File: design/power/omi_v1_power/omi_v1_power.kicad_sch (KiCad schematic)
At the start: 0 parts

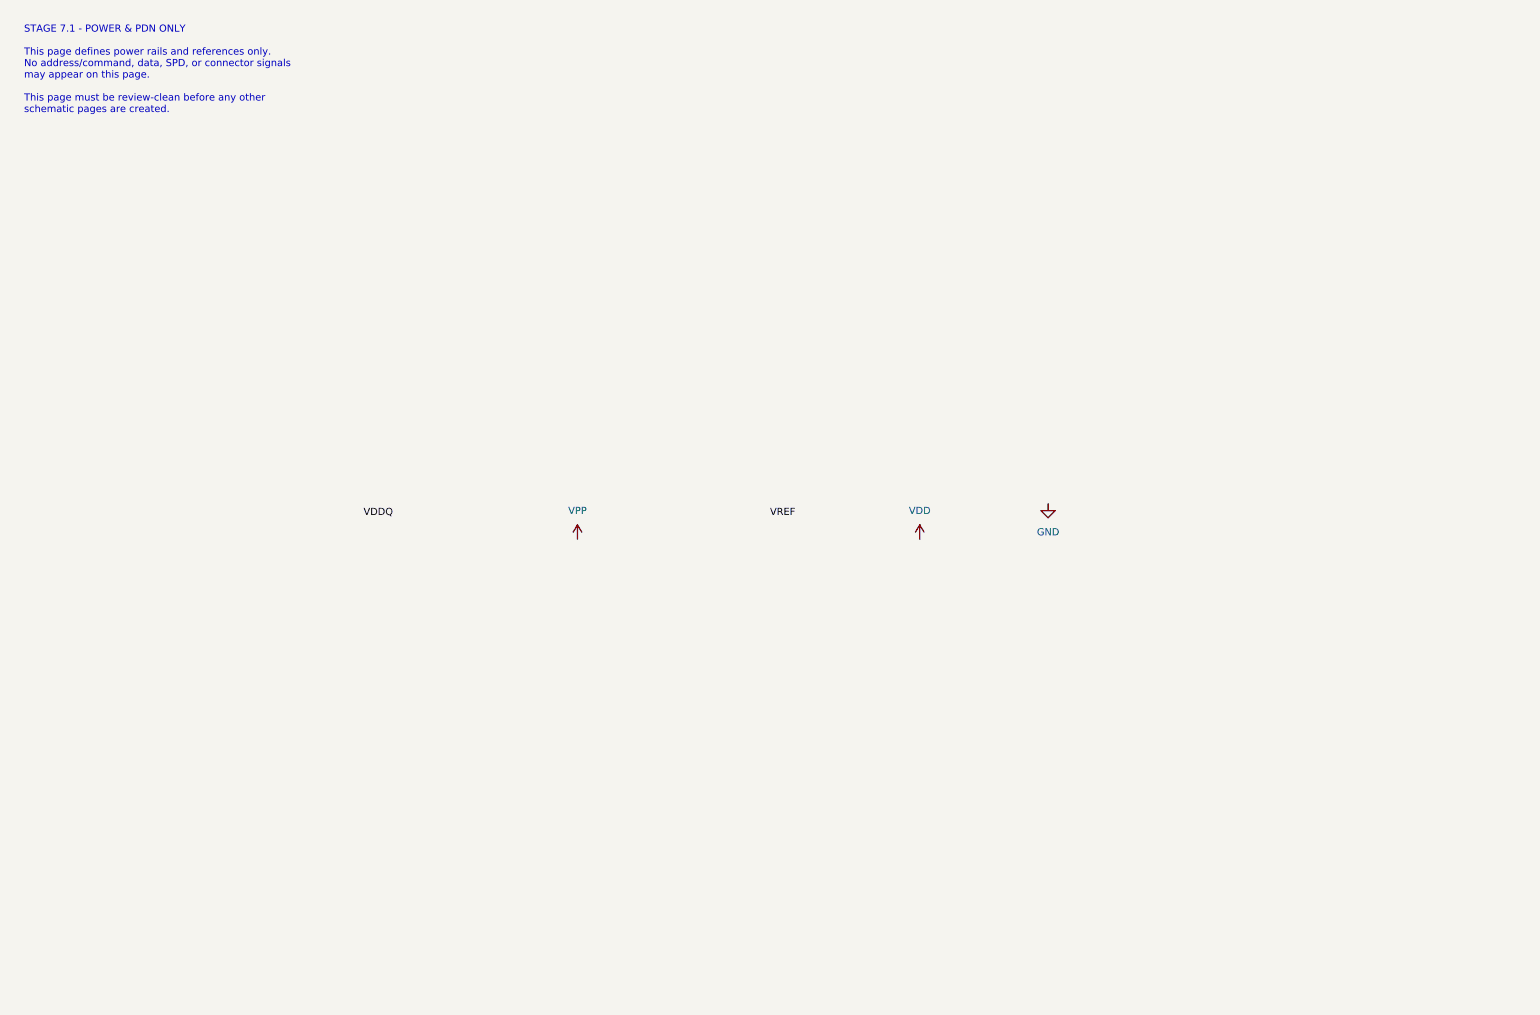
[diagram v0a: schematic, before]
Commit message: feat: add initial OMI v1 power and PDN schematic with PDF documentation
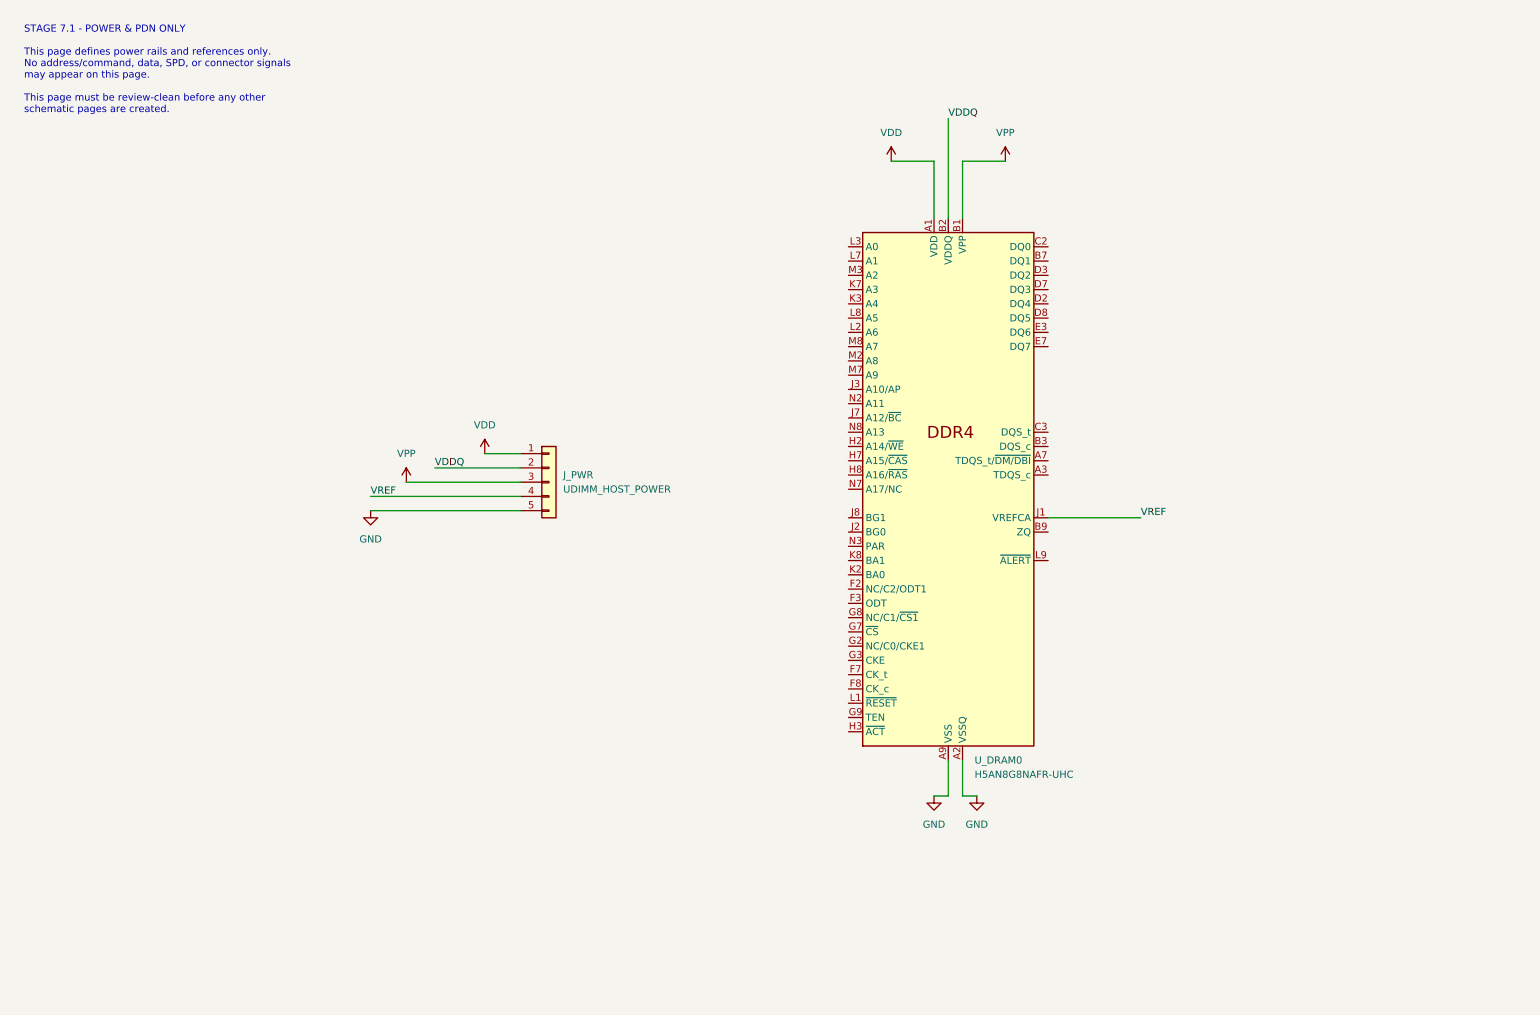
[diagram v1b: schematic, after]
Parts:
- added J_PWR: UDIMM_HOST_POWER, symbol Connector_Generic:Conn_01x05
- added U_DRAM0: H5AN8G8NAFR-UHC, Package_BGA:FBGA-78_7.5x11mm_Layout2x3x13_P0.8mm, symbol Memory_RAM:H5AN8G8NAFR-UHC
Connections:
- net GND: now also J_PWR.5 (Pin_5), U_DRAM0.A2 (VSSQ), U_DRAM0.A8 (VSSQ), U_DRAM0.A9 (VSS), U_DRAM0.C8 (VSS), U_DRAM0.D1 (VSSQ), U_DRAM0.D9 (VSSQ), U_DRAM0.E1 (VSS), U_DRAM0.E9 (VSS), U_DRAM0.G1 (VSS), U_DRAM0.H9 (VSS), U_DRAM0.K1 (VSS), U_DRAM0.K9 (VSS), U_DRAM0.N1 (VSS)
- net VDD: now also J_PWR.1 (Pin_1), U_DRAM0.A1 (VDD), U_DRAM0.C7 (VDD), U_DRAM0.F1 (VDD), U_DRAM0.F9 (VDD), U_DRAM0.H1 (VDD), U_DRAM0.J9 (VDD), U_DRAM0.M1 (VDD), U_DRAM0.N9 (VDD)
- net VDDQ: now also J_PWR.2 (Pin_2), U_DRAM0.B2 (VDDQ), U_DRAM0.B8 (VDDQ), U_DRAM0.C1 (VDDQ), U_DRAM0.C9 (VDDQ), U_DRAM0.E2 (VDDQ), U_DRAM0.E8 (VDDQ)
- net VPP: now also J_PWR.3 (Pin_3), U_DRAM0.B1 (VPP), U_DRAM0.M9 (VPP)
- net VREF: now also J_PWR.4 (Pin_4), U_DRAM0.J1 (VREFCA)

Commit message: feat: Add OMI v1 Stage 7.1 Power & PDN final documentation and PDF artifact.
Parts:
- added U_DRAM1, U_DRAM2, U_DRAM3, U_DRAM4, U_DRAM5, U_DRAM6, U_DRAM7: H5AN8G8NAFR-UHC, Package_BGA:FBGA-78_7.5x11mm_Layout2x3x13_P0.8mm, symbol Memory_RAM:H5AN8G8NAFR-UHC
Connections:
- net GND: now also U_DRAM1.A2 (VSSQ), U_DRAM1.A8 (VSSQ), U_DRAM1.A9 (VSS), U_DRAM1.C8 (VSS), U_DRAM1.D1 (VSSQ), U_DRAM1.D9 (VSSQ), U_DRAM1.E1 (VSS), U_DRAM1.E9 (VSS), U_DRAM1.G1 (VSS), U_DRAM1.H9 (VSS), U_DRAM1.K1 (VSS), U_DRAM1.K9 (VSS), U_DRAM1.N1 (VSS), U_DRAM2.A2 (VSSQ), U_DRAM2.A8 (VSSQ), U_DRAM2.A9 (VSS), U_DRAM2.C8 (VSS), U_DRAM2.D1 (VSSQ), U_DRAM2.D9 (VSSQ), U_DRAM2.E1 (VSS), U_DRAM2.E9 (VSS), U_DRAM2.G1 (VSS), U_DRAM2.H9 (VSS), U_DRAM2.K1 (VSS), U_DRAM2.K9 (VSS), U_DRAM2.N1 (VSS), U_DRAM3.A2 (VSSQ), U_DRAM3.A8 (VSSQ), U_DRAM3.A9 (VSS), U_DRAM3.C8 (VSS), U_DRAM3.D1 (VSSQ), U_DRAM3.D9 (VSSQ), U_DRAM3.E1 (VSS), U_DRAM3.E9 (VSS), U_DRAM3.G1 (VSS), U_DRAM3.H9 (VSS), U_DRAM3.K1 (VSS), U_DRAM3.K9 (VSS), U_DRAM3.N1 (VSS), U_DRAM4.A2 (VSSQ), U_DRAM4.A8 (VSSQ), U_DRAM4.A9 (VSS), U_DRAM4.C8 (VSS), U_DRAM4.D1 (VSSQ), U_DRAM4.D9 (VSSQ), U_DRAM4.E1 (VSS), U_DRAM4.E9 (VSS), U_DRAM4.G1 (VSS), U_DRAM4.H9 (VSS), U_DRAM4.K1 (VSS), U_DRAM4.K9 (VSS), U_DRAM4.N1 (VSS), U_DRAM5.A2 (VSSQ), U_DRAM5.A8 (VSSQ), U_DRAM5.A9 (VSS), U_DRAM5.C8 (VSS), U_DRAM5.D1 (VSSQ), U_DRAM5.D9 (VSSQ), U_DRAM5.E1 (VSS), U_DRAM5.E9 (VSS), U_DRAM5.G1 (VSS), U_DRAM5.H9 (VSS), U_DRAM5.K1 (VSS), U_DRAM5.K9 (VSS), U_DRAM5.N1 (VSS), U_DRAM6.A2 (VSSQ), U_DRAM6.A8 (VSSQ), U_DRAM6.A9 (VSS), U_DRAM6.C8 (VSS), U_DRAM6.D1 (VSSQ), U_DRAM6.D9 (VSSQ), U_DRAM6.E1 (VSS), U_DRAM6.E9 (VSS), U_DRAM6.G1 (VSS), U_DRAM6.H9 (VSS), U_DRAM6.K1 (VSS), U_DRAM6.K9 (VSS), U_DRAM6.N1 (VSS), U_DRAM7.A2 (VSSQ), U_DRAM7.A8 (VSSQ), U_DRAM7.A9 (VSS), U_DRAM7.C8 (VSS), U_DRAM7.D1 (VSSQ), U_DRAM7.D9 (VSSQ), U_DRAM7.E1 (VSS), U_DRAM7.E9 (VSS), U_DRAM7.G1 (VSS), U_DRAM7.H9 (VSS), U_DRAM7.K1 (VSS), U_DRAM7.K9 (VSS), U_DRAM7.N1 (VSS)
- net VDD: now also U_DRAM1.A1 (VDD), U_DRAM1.C7 (VDD), U_DRAM1.F1 (VDD), U_DRAM1.F9 (VDD), U_DRAM1.H1 (VDD), U_DRAM1.J9 (VDD), U_DRAM1.M1 (VDD), U_DRAM1.N9 (VDD), U_DRAM2.A1 (VDD), U_DRAM2.C7 (VDD), U_DRAM2.F1 (VDD), U_DRAM2.F9 (VDD), U_DRAM2.H1 (VDD), U_DRAM2.J9 (VDD), U_DRAM2.M1 (VDD), U_DRAM2.N9 (VDD), U_DRAM3.A1 (VDD), U_DRAM3.C7 (VDD), U_DRAM3.F1 (VDD), U_DRAM3.F9 (VDD), U_DRAM3.H1 (VDD), U_DRAM3.J9 (VDD), U_DRAM3.M1 (VDD), U_DRAM3.N9 (VDD), U_DRAM4.A1 (VDD), U_DRAM4.C7 (VDD), U_DRAM4.F1 (VDD), U_DRAM4.F9 (VDD), U_DRAM4.H1 (VDD), U_DRAM4.J9 (VDD), U_DRAM4.M1 (VDD), U_DRAM4.N9 (VDD), U_DRAM5.A1 (VDD), U_DRAM5.C7 (VDD), U_DRAM5.F1 (VDD), U_DRAM5.F9 (VDD), U_DRAM5.H1 (VDD), U_DRAM5.J9 (VDD), U_DRAM5.M1 (VDD), U_DRAM5.N9 (VDD), U_DRAM6.A1 (VDD), U_DRAM6.C7 (VDD), U_DRAM6.F1 (VDD), U_DRAM6.F9 (VDD), U_DRAM6.H1 (VDD), U_DRAM6.J9 (VDD), U_DRAM6.M1 (VDD), U_DRAM6.N9 (VDD), U_DRAM7.A1 (VDD), U_DRAM7.C7 (VDD), U_DRAM7.F1 (VDD), U_DRAM7.F9 (VDD), U_DRAM7.H1 (VDD), U_DRAM7.J9 (VDD), U_DRAM7.M1 (VDD), U_DRAM7.N9 (VDD)
- net VDDQ: now also U_DRAM1.B2 (VDDQ), U_DRAM1.B8 (VDDQ), U_DRAM1.C1 (VDDQ), U_DRAM1.C9 (VDDQ), U_DRAM1.E2 (VDDQ), U_DRAM1.E8 (VDDQ), U_DRAM2.B2 (VDDQ), U_DRAM2.B8 (VDDQ), U_DRAM2.C1 (VDDQ), U_DRAM2.C9 (VDDQ), U_DRAM2.E2 (VDDQ), U_DRAM2.E8 (VDDQ), U_DRAM3.B2 (VDDQ), U_DRAM3.B8 (VDDQ), U_DRAM3.C1 (VDDQ), U_DRAM3.C9 (VDDQ), U_DRAM3.E2 (VDDQ), U_DRAM3.E8 (VDDQ), U_DRAM4.B2 (VDDQ), U_DRAM4.B8 (VDDQ), U_DRAM4.C1 (VDDQ), U_DRAM4.C9 (VDDQ), U_DRAM4.E2 (VDDQ), U_DRAM4.E8 (VDDQ), U_DRAM5.B2 (VDDQ), U_DRAM5.B8 (VDDQ), U_DRAM5.C1 (VDDQ), U_DRAM5.C9 (VDDQ), U_DRAM5.E2 (VDDQ), U_DRAM5.E8 (VDDQ), U_DRAM6.B2 (VDDQ), U_DRAM6.B8 (VDDQ), U_DRAM6.C1 (VDDQ), U_DRAM6.C9 (VDDQ), U_DRAM6.E2 (VDDQ), U_DRAM6.E8 (VDDQ), U_DRAM7.B2 (VDDQ), U_DRAM7.B8 (VDDQ), U_DRAM7.C1 (VDDQ), U_DRAM7.C9 (VDDQ), U_DRAM7.E2 (VDDQ), U_DRAM7.E8 (VDDQ)
- net VPP: now also U_DRAM1.B1 (VPP), U_DRAM1.M9 (VPP), U_DRAM2.B1 (VPP), U_DRAM2.M9 (VPP), U_DRAM3.B1 (VPP), U_DRAM3.M9 (VPP), U_DRAM4.B1 (VPP), U_DRAM4.M9 (VPP), U_DRAM5.B1 (VPP), U_DRAM5.M9 (VPP), U_DRAM6.B1 (VPP), U_DRAM6.M9 (VPP), U_DRAM7.B1 (VPP), U_DRAM7.M9 (VPP)
- net VREF: now also U_DRAM1.J1 (VREFCA), U_DRAM2.J1 (VREFCA), U_DRAM3.J1 (VREFCA), U_DRAM4.J1 (VREFCA), U_DRAM5.J1 (VREFCA), U_DRAM6.J1 (VREFCA), U_DRAM7.J1 (VREFCA)
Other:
- moved on the sheet: J_PWR, U_DRAM0
